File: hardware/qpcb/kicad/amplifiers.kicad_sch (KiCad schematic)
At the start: 0 parts

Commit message: Add mixer footprint and symbols
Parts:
- added U11, U12, U13, U14, U15, U16, U17, U18, U19, U6: ~, symbol RF_mount_PCBs:tsy_83ln+_amplifier
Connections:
- new net 6V: U11.1 (VDD), U11.2 (VDD), U11.3 (VDD), U11.4 (VDD), U12.1 (VDD), U12.2 (VDD), U12.3 (VDD), U12.4 (VDD), U13.1 (VDD), U13.2 (VDD), U13.3 (VDD), U13.4 (VDD), U14.1 (VDD), U14.2 (VDD), U14.3 (VDD), U14.4 (VDD), U15.1 (VDD), U15.2 (VDD), U15.3 (VDD), U15.4 (VDD), U16.1 (VDD), U16.2 (VDD), U16.3 (VDD), U16.4 (VDD), U17.1 (VDD), U17.2 (VDD), U17.3 (VDD), U17.4 (VDD), U18.1 (VDD), U18.2 (VDD), U18.3 (VDD), U18.4 (VDD), U19.1 (VDD), U19.2 (VDD), U19.3 (VDD), U19.4 (VDD), U6.1 (VDD), U6.2 (VDD), U6.3 (VDD), U6.4 (VDD)
- new net GND: U11.5 (GND), U11.6 (GND), U11.7 (GND), U11.8 (GND), U12.5 (GND), U12.6 (GND), U12.7 (GND), U12.8 (GND), U13.5 (GND), U13.6 (GND), U13.7 (GND), U13.8 (GND), U14.5 (GND), U14.6 (GND), U14.7 (GND), U14.8 (GND), U15.5 (GND), U15.6 (GND), U15.7 (GND), U15.8 (GND), U16.5 (GND), U16.6 (GND), U16.7 (GND), U16.8 (GND), U17.5 (GND), U17.6 (GND), U17.7 (GND), U17.8 (GND), U18.5 (GND), U18.6 (GND), U18.7 (GND), U18.8 (GND), U19.5 (GND), U19.6 (GND), U19.7 (GND), U19.8 (GND), U6.5 (GND), U6.6 (GND), U6.7 (GND), U6.8 (GND)
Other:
- note added: "Amplifiers"
- note added: "External connections"

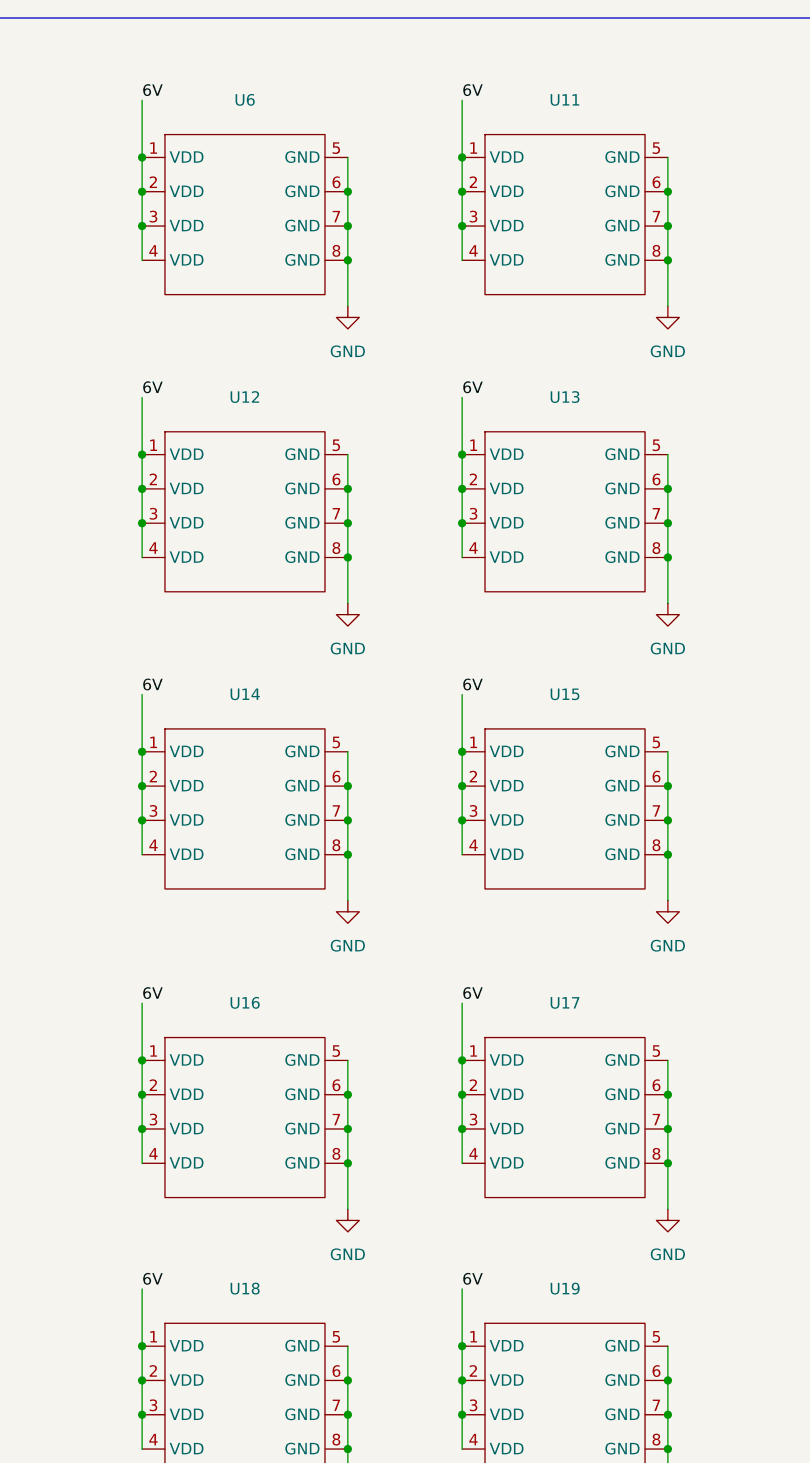
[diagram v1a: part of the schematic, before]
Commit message: Final version of MC43063A and fill components' production info
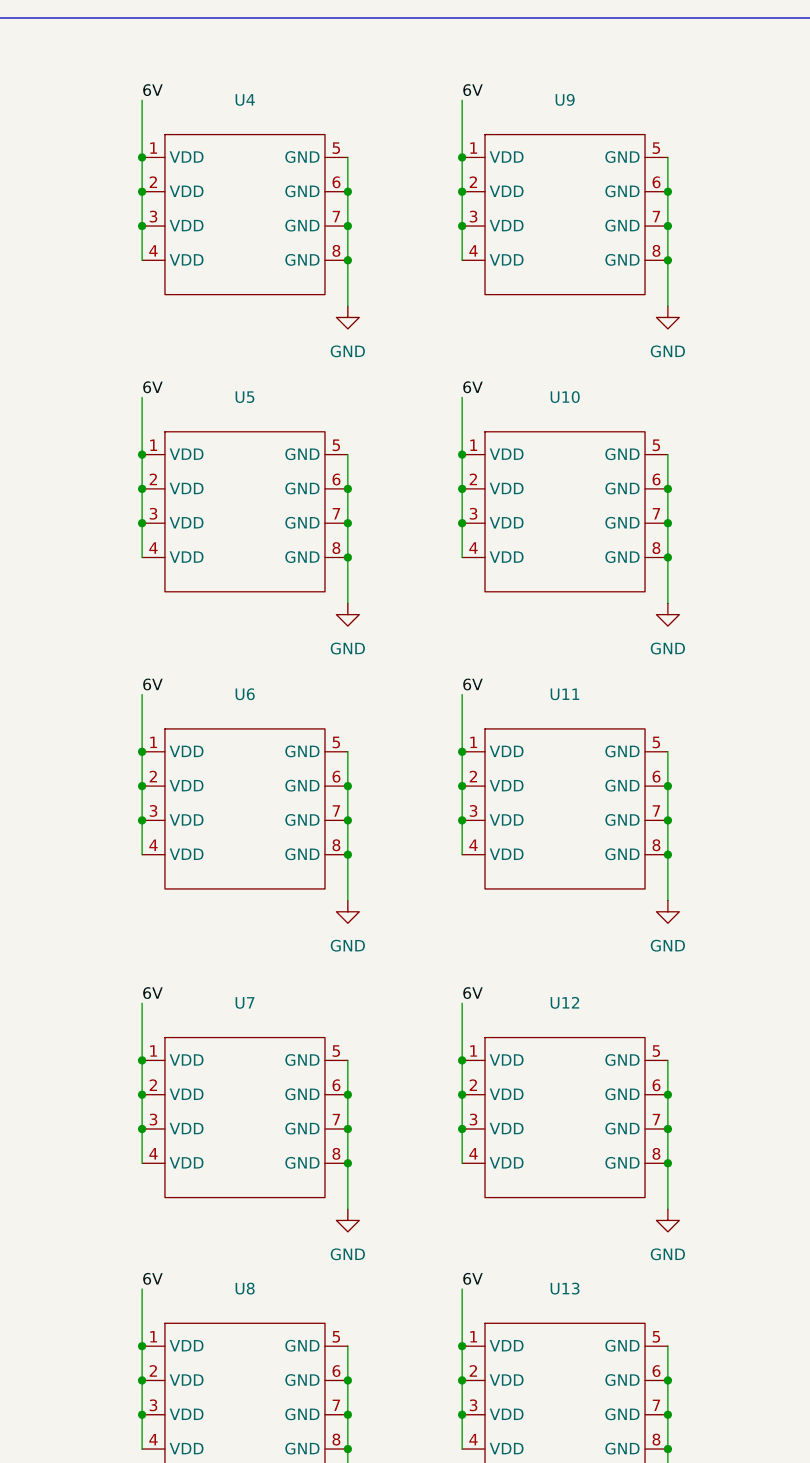
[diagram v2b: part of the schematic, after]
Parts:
- renumbered U13 to U10, U15 to U11, U17 to U12, U19 to U13, U6 to U4, U12 to U5, U14 to U6, U16 to U7, U18 to U8, U11 to U9

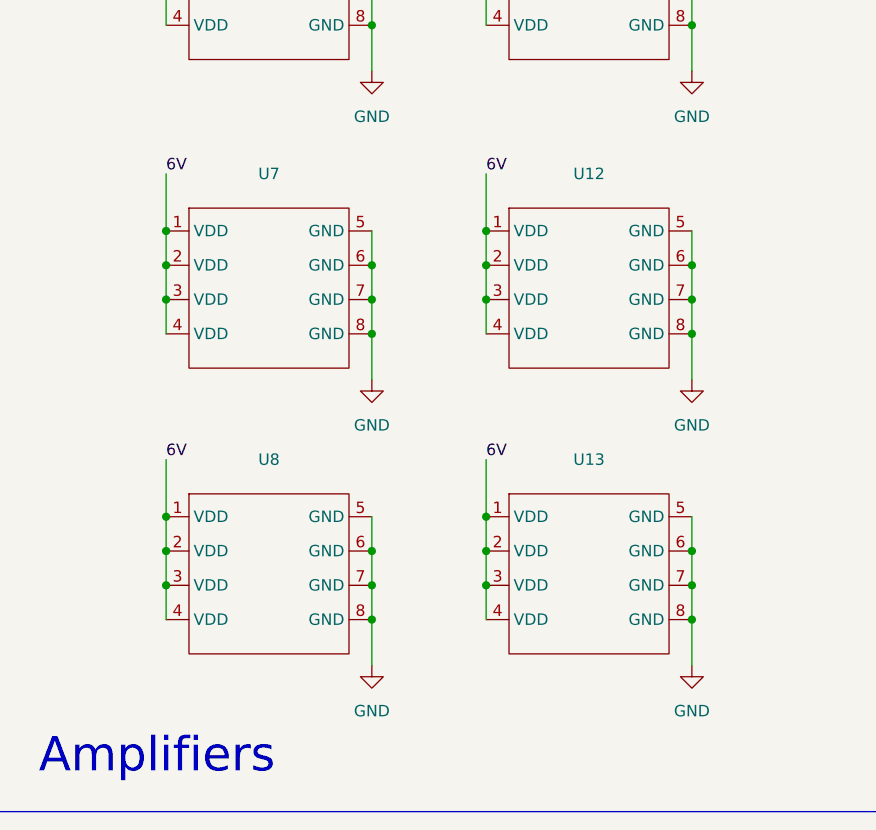
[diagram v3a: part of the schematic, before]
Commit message: Add final footprints of daughter boards, change components for -3v3 power supply line and placement almost finished
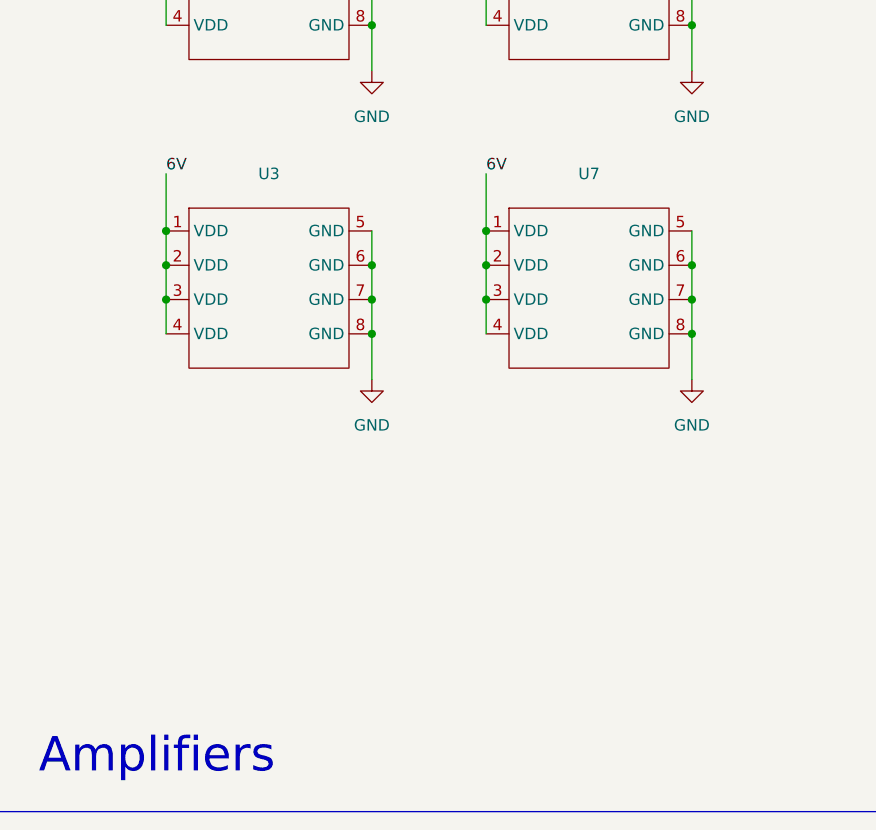
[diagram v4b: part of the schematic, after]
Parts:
- removed U12, U13, U8: ~, symbol RF_mount_PCBs:tsy_83ln+_amplifier
- added U3: ~, footprints:tsy_83ln+_amplifier, symbol RF_mount_PCBs:tsy_83ln+_amplifier
- U10, U11, U4, U5, U6, U7, U9: footprint (none) -> footprints:tsy_83ln+_amplifier
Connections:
- net 6V: now also U3.1 (VDD), U3.2 (VDD), U3.3 (VDD), U3.4 (VDD)
- net GND: now also U3.5 (GND), U3.6 (GND), U3.7 (GND), U3.8 (GND)
